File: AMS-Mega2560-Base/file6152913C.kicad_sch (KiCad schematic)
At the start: 14 parts, among them IC16 DS3231SN#, IC17 MAX232CPE+, IC19 MAX6326UR31+T, Q24 BS250, U3 S8411-45R

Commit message: pushing this change to the repo need to vet some schematics
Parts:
- removed R64: 4.7K, Resistor_THT:R_Axial_DIN0207_L6.3mm_D2.5mm_P2.54mm_Vertical, symbol Device:R
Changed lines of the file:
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@@
 (kicad_sch (version 20211123) (generator eeschema)
   (paper "A4")
-  (junction (at 104.14 67.31) (diameter 0) (color 0 0 0 0)
-  )
   (junction (at 226.695 31.75) (diameter 0) (color 0 0 0 0)
   )
@@
   (junction (at 33.02 55.88) (diameter 0) (color 0 0 0 0)
   )
-  (junction (at 88.265 83.185) (diameter 0) (color 0 0 0 0)
+  (junction (at 68.58 55.88) (diameter 0) (color 0 0 0 0)
+  )
+  (junction (at 68.58 58.42) (diameter 0) (color 0 0 0 0)
+  )
+  (junction (at 21.59 43.18) (diameter 0) (color 0 0 0 0)
+  )
+  (junction (at 76.2 43.18) (diameter 0) (color 0 0 0 0)
+  )
+  (junction (at 225.425 53.34) (diameter 0) (color 0 0 0 0)
+  )
+  (junction (at 33.02 58.42) (diameter 0) (color 0 0 0 0)
   )
   (junction (at 126.365 67.31) (diameter 0) (color 0 0 0 0)
-  )
-  (junction (at 68.58 55.88) (diameter 0) (color 0 0 0 0)
-  )
-  (junction (at 68.58 58.42) (diameter 0) (color 0 0 0 0)
-  )
-  (junction (at 21.59 43.18) (diameter 0) (color 0 0 0 0)
-  )
-  (junction (at 76.2 43.18) (diameter 0) (color 0 0 0 0)
-  )
-  (junction (at 225.425 53.34) (diameter 0) (color 0 0 0 0)
-  )
-  (junction (at 33.02 58.42) (diameter 0) (color 0 0 0 0)
   )
   (junction (at 133.985 67.31) (diameter 0) (color 0 0 0 0)
@@
     (stroke (width 0) (type default) (color 0 0 0 0))
   )
-  (wire (pts (xy 104.14 67.31) (xy 126.365 67.31))
-    (stroke (width 0) (type default) (color 0 0 0 0))
-  )
   (wire (pts (xy 69.85 31.75) (xy 69.85 40.64))
     (stroke (width 0) (type default) (color 0 0 0 0))
@@
     (stroke (width 0) (type default) (color 0 0 0 0))
   )
-  (wire (pts (xy 88.265 83.185) (xy 88.265 74.93))
-    (stroke (width 0) (type default) (color 0 0 0 0))
-  )
   (wire (pts (xy 33.02 62.23) (xy 33.02 58.42))
     (stroke (width 0) (type default) (color 0 0 0 0))
@@
     (stroke (width 0) (type default) (color 0 0 0 0))
   )
+  (wire (pts (xy 126.365 64.77) (xy 126.365 67.31))
+    (stroke (width 0) (type default) (color 0 0 0 0))
+  )
   (wire (pts (xy 68.58 58.42) (xy 68.58 55.88))
     (stroke (width 0) (type default) (color 0 0 0 0))
@@
   )
   (wire (pts (xy 69.85 24.13) (xy 69.85 20.32))
-    (stroke (width 0) (type default) (color 0 0 0 0))
-  )
-  (wire (pts (xy 88.265 67.31) (xy 104.14 67.31))
     (stroke (width 0) (type default) (color 0 0 0 0))
   )
@@
     (pin "1")
   )
-  (symbol (lib_id "power:+3.3VP") (at 104.14 67.31 0) (unit 1)
-    (in_bom yes) (on_board yes)
-    (property "Reference" "#PWR0138" (id 0) (at 107.95 68.58 0)
-      (effects (font (size 1.27 1.27)) hide)
-    )
-    (property "Value" "+3.3VP" (id 1) (at 104.521 62.9158 0))
-    (property "Footprint" "" (id 2) (at 104.14 67.31 0)
-      (effects (font (size 1.27 1.27)) hide)
-    )
-    (property "Datasheet" "" (id 3) (at 104.14 67.31 0)
+  (symbol (lib_id "power:+3.3VP") (at 126.365 64.77 0) (unit 1)
+    (in_bom yes) (on_board yes)
+    (property "Reference" "#PWR0138" (id 0) (at 130.175 66.04 0)
+      (effects (font (size 1.27 1.27)) hide)
+    )
+    (property "Value" "+3.3VP" (id 1) (at 126.746 60.3758 0))
+    (property "Footprint" "" (id 2) (at 126.365 64.77 0)
+      (effects (font (size 1.27 1.27)) hide)
+    )
+    (property "Datasheet" "" (id 3) (at 126.365 64.77 0)
       (effects (font (size 1.27 1.27)) hide)
     )
@@
     (pin "3")
   )
-  (symbol (lib_id "Device:R") (at 88.265 71.12 0) (unit 1)
-    (in_bom yes) (on_board yes)
-    (property "Reference" "R64" (id 0) (at 90.043 69.9516 0)
-      (effects (font (size 1.27 1.27)) (justify left))
-    )
-    (property "Value" "4.7K" (id 1) (at 90.043 72.263 0)
-      (effects (font (size 1.27 1.27)) (justify left))
-    )
-    (property "Footprint" "Resistor_THT:R_Axial_DIN0207_L6.3mm_D2.5mm_P2.54mm_Vertical" (id 2) (at 86.487 71.12 90)
-      (effects (font (size 1.27 1.27)) hide)
-    )
-    (property "Datasheet" "~" (id 3) (at 88.265 71.12 0)
-      (effects (font (size 1.27 1.27)) hide)
-    )
-    (pin "1")
-    (pin "2")
-  )
   (symbol (lib_id "Transistor_FET:BS250") (at 94.615 97.155 90) (mirror x) (unit 1)

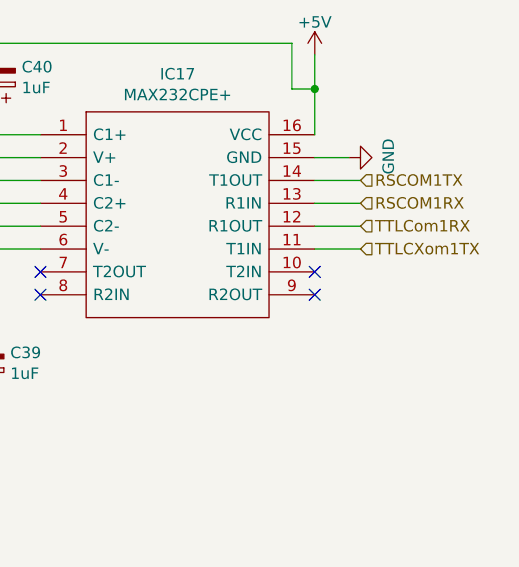
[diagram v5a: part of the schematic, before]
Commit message: working on fixing the screw ups. adding a second serial port
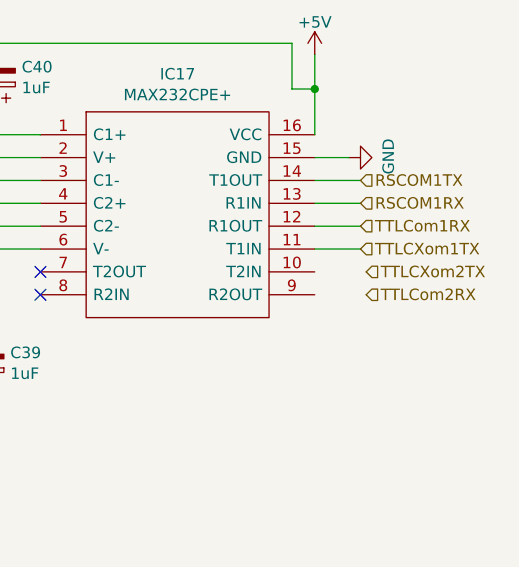
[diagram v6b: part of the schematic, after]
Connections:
- no-connect marks 7 -> 5
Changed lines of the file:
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@@
   (junction (at 69.85 40.64) (diameter 0) (color 0 0 0 0)
   )
-  (no_connect (at 262.255 48.26))
   (no_connect (at 33.02 45.72))
   (no_connect (at 33.02 40.64))
   (no_connect (at 231.775 48.26))
   (no_connect (at 231.775 50.8))
-  (no_connect (at 262.255 50.8))
   (no_connect (at 33.02 48.26))
   (wire (pts (xy 221.615 40.64) (xy 221.615 38.1))
@@
     (effects (font (size 1.27 1.27)) (justify left))
   )
+  (hierarchical_label "TTLCXom2TX" (shape input) (at 267.97 48.26 0)
+    (effects (font (size 1.27 1.27)) (justify left))
+  )
   (hierarchical_label "RTCBattLevel" (shape input) (at 85.09 93.345 90)
     (effects (font (size 1.27 1.27)) (justify left))
@@
     (effects (font (size 1.27 1.27)) (justify left))
   )
+  (hierarchical_label "TTLCom2RX" (shape input) (at 267.97 50.8 0)
+    (effects (font (size 1.27 1.27)) (justify left))
+  )

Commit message: still working on the base code. updating some of the HW stuff
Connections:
- net TTLCXom2TX: now also IC17.10 (T2IN)
- net TTLCom2RX: now also IC17.9 (R2OUT)
- net RSCOM2TX: now reaches IC17.7 (T2OUT)
- net RSCOM2RX: now reaches IC17.8 (R2IN)
- no-connect marks 5 -> 3
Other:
- moved on the sheet: C37, C38, C39, C40, IC17

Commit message: updating this for the merge.
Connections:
- net RSCOM2RX: no longer names the net of IC17.8 (R2IN)
- net RSCOM2TX: no longer names the net of IC17.7 (T2OUT)
- net TTLCXom2TX: no longer names the net of IC17.10 (T2IN)
- net TTLCom2RX: no longer names the net of IC17.9 (R2OUT)
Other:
- moved on the sheet: C37, C38, C39, C40, IC17
